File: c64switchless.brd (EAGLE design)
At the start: 22.8 x 45.4 mm, 12 parts, among them IC1 27C256, IC2 PIC12F629P

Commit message: updated with license
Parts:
- renumbered U$1 to SV4
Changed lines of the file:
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@@
 <attribute name="VALUE" x="-0.127" y="41.148" size="1.27" layer="27" ratio="10" rot="R270" display="off"/>
 </element>
-<element name="U$1" library="microchip" package="ICSP_MICROCHIP" value="ICSP_MICROCHIP" x="7.62" y="17.78" smashed="yes" rot="MR180">
+<element name="SV4" library="microchip" package="ICSP_MICROCHIP" value="ICSP_MICROCHIP" x="7.62" y="17.78" smashed="yes" rot="MR180">
 <attribute name="NAME" x="6.35" y="9.779" size="1.27" layer="26" ratio="10" rot="MR180" display="off"/>
 <attribute name="VALUE" x="6.35" y="27.051" size="1.27" layer="28" ratio="10" rot="MR180" display="off"/>
@@
 <vertex x="0" y="-1.27"/>
 </polygon>
-<contactref element="U$1" pad="3"/>
+<contactref element="SV4" pad="3"/>
 <polygon width="0.3048" layer="1" isolate="0.4064">
 <vertex x="0" y="44.45"/>
@@
 <wire x1="15.24" y1="35.56" x2="17.78" y2="35.56" width="0.8128" layer="16"/>
 <wire x1="5.08" y1="40.64" x2="17.78" y2="40.64" width="0.8128" layer="16"/>
-<contactref element="U$1" pad="2"/>
+<contactref element="SV4" pad="2"/>
 <wire x1="7.62" y1="13.97" x2="11.43" y2="17.78" width="0.254" layer="1"/>
 <wire x1="11.43" y1="17.78" x2="11.43" y2="31.75" width="0.254" layer="1"/>
@@
 <contactref element="IC2" pad="6"/>
 <contactref element="PAD2" pad="1"/>
-<contactref element="U$1" pad="5"/>
+<contactref element="SV4" pad="5"/>
 <wire x1="8.89" y1="29.21" x2="7.62" y2="30.48" width="0.1524" layer="1"/>
 <wire x1="8.89" y1="22.86" x2="8.89" y2="29.21" width="0.1524" layer="1"/>
@@
 <signal name="#RESTORE">
 <contactref element="PAD1" pad="1"/>
-<contactref element="U$1" pad="1"/>
+<contactref element="SV4" pad="1"/>
 <contactref element="IC2" pad="4"/>
 <wire x1="15.24" y1="27.94" x2="15.24" y2="22.86" width="0.254" layer="1"/>
@@
 </signal>
 <signal name="N$1">
-<contactref element="U$1" pad="4"/>
+<contactref element="SV4" pad="4"/>
 <contactref element="IC2" pad="7"/>
 <wire x1="6.35" y1="31.75" x2="7.62" y2="33.02" width="0.1524" layer="1"/>

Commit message: hole sizes
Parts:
- moved PAD2 0.32 mm to (5.40, 0.64)
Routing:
- net GND: track 2.54 -> 8.57 mm, vias 0 -> 2
- net N$1: track 15.0 -> 20.8 mm
- net N$22: track 10.2 -> 8.67 mm
- net N$24: track 30.6 -> 31.5 mm
- removed copper zone on layer 1, net GND
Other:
- board text added: "Rev 1.12"
- board text removed: "Rev 1.11"
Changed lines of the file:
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@@
 <text x="13.97" y="42.545" size="0.8128" layer="21" font="fixed" ratio="29">BWACK 2016</text>
 <text x="1.27" y="3.175" size="0.6096" layer="21" font="fixed">Quad Kernal Switch</text>
-<text x="1.27" y="-0.215" size="0.6096" layer="21">RESET</text>
+<text x="1.016" y="-0.215" size="0.6096" layer="21">RESET</text>
 <text x="9.525" y="-0.135" size="0.6096" layer="21">Restore</text>
 <text x="19.05" y="0" size="0.6096" layer="21" font="fixed" rot="R180">RGB LEDs</text>
-<text x="1.27" y="1.905" size="0.6096" layer="21" font="fixed">Rev 1.11</text>
+<text x="1.27" y="1.905" size="0.6096" layer="21" font="fixed">Rev 1.12</text>
 <text x="18.8595" y="5.3975" size="0.6096" layer="21" font="fixed">RED</text>
 <text x="13.2715" y="5.3975" size="0.6096" layer="21" font="fixed">GREEN</text>
@@
 <attribute name="VALUE" x="8.255" y="1.235" size="0.0254" layer="27"/>
 </element>
-<element name="PAD2" library="wirepad" package="1,6/0,9" value="" x="5.715" y="0.635" smashed="yes">
-<attribute name="NAME" x="4.953" y="1.651" size="0.6096" layer="25" ratio="10" display="off"/>
-<attribute name="VALUE" x="5.715" y="1.235" size="0.0254" layer="27"/>
+<element name="PAD2" library="wirepad" package="1,6/0,9" value="" x="5.3975" y="0.635" smashed="yes">
+<attribute name="NAME" x="4.6355" y="1.651" size="0.6096" layer="25" ratio="10" display="off"/>
+<attribute name="VALUE" x="5.3975" y="1.235" size="0.0254" layer="27"/>
 </element>
 <element name="R1" library="rcl" package="0207/10" value="2k" x="12.7" y="15.24" smashed="yes" rot="R90">
@@
 <contactref element="IC1" pad="20"/>
 <wire x1="2.54" y1="7.62" x2="5.08" y2="7.62" width="0.4064" layer="16"/>
-<polygon width="0.4064" layer="16" isolate="0.4064">
+<polygon width="0.4064" layer="16" isolate="0.3048">
 <vertex x="0" y="44.45"/>
 <vertex x="22.86" y="44.45"/>
@@
 </polygon>
 <contactref element="SV4" pad="3"/>
-<polygon width="0.3048" layer="1" isolate="0.4064">
-<vertex x="0" y="44.45"/>
-<vertex x="22.86" y="44.45"/>
-<vertex x="22.86" y="-1.27"/>
-<vertex x="0" y="-1.27"/>
-</polygon>
 <contactref element="SV3" pad="3"/>
 <contactref element="SV3" pad="4"/>
+<wire x1="10.16" y1="42.8625" x2="10.16" y2="39.37" width="1.27" layer="1"/>
+<wire x1="10.16" y1="39.37" x2="7.62" y2="39.37" width="1.27" layer="1"/>
+<via x="10.16" y="42.8625" extent="1-16" drill="0.6" shape="square"/>
+<via x="7.62" y="39.37" extent="1-16" drill="0.6" shape="square"/>
 </signal>
 <signal name="VCC">
@@
 <wire x1="5.08" y1="40.64" x2="17.78" y2="40.64" width="0.8128" layer="16"/>
 <contactref element="SV4" pad="2"/>
-<wire x1="7.62" y1="13.97" x2="11.43" y2="17.78" width="0.254" layer="1"/>
-<wire x1="11.43" y1="17.78" x2="11.43" y2="31.75" width="0.254" layer="1"/>
-<wire x1="11.43" y1="31.75" x2="15.24" y2="35.56" width="0.254" layer="1"/>
+<wire x1="7.62" y1="13.97" x2="11.43" y2="17.78" width="0.1524" layer="1"/>
+<wire x1="11.43" y1="17.78" x2="11.43" y2="31.75" width="0.1524" layer="1"/>
+<wire x1="11.43" y1="31.75" x2="15.24" y2="35.56" width="0.1524" layer="1"/>
 </signal>
 <signal name="N$2">
@@
 <wire x1="16.51" y1="39.37" x2="15.24" y2="38.1" width="0.1524" layer="1"/>
 <wire x1="21.59" y1="39.37" x2="16.51" y2="39.37" width="0.1524" layer="1"/>
-<wire x1="21.59" y1="32.385" x2="21.59" y2="39.37" width="0.1524" layer="1"/>
-<wire x1="19.05" y1="31.115" x2="21.59" y2="32.385" width="0.1524" layer="1"/>
-<wire x1="19.05" y1="29.21" x2="19.05" y2="31.115" width="0.1524" layer="1"/>
+<wire x1="21.59" y1="31.75" x2="21.59" y2="39.37" width="0.1524" layer="1"/>
+<wire x1="19.05" y1="31.75" x2="21.59" y2="31.75" width="0.1524" layer="1"/>
+<wire x1="19.05" y1="29.21" x2="19.05" y2="31.75" width="0.1524" layer="1"/>
 <wire x1="17.78" y1="27.94" x2="19.05" y2="29.21" width="0.1524" layer="1"/>
 </signal>
@@
 <contactref element="PAD2" pad="1"/>
 <contactref element="SV4" pad="5"/>
-<wire x1="8.89" y1="29.21" x2="7.62" y2="30.48" width="0.1524" layer="1"/>
-<wire x1="8.89" y1="22.86" x2="8.89" y2="29.21" width="0.1524" layer="1"/>
-<wire x1="7.62" y1="21.59" x2="8.89" y2="22.86" width="0.1524" layer="1"/>
-<wire x1="3.81" y1="2.54" x2="5.715" y2="0.635" width="0.254" layer="1"/>
-<wire x1="3.81" y1="2.54" x2="3.81" y2="16.51" width="0.254" layer="1"/>
-<wire x1="3.81" y1="16.51" x2="6.35" y2="16.51" width="0.254" layer="1"/>
-<wire x1="6.35" y1="16.51" x2="6.35" y2="17.78" width="0.254" layer="1"/>
-<wire x1="6.35" y1="17.78" x2="8.89" y2="17.78" width="0.254" layer="1"/>
-<wire x1="8.89" y1="17.78" x2="8.89" y2="20.32" width="0.254" layer="1"/>
-<wire x1="8.89" y1="20.32" x2="7.62" y2="21.59" width="0.254" layer="1"/>
+<wire x1="3.81" y1="2.54" x2="5.3975" y2="0.635" width="0.1524" layer="1"/>
+<wire x1="3.81" y1="2.54" x2="3.81" y2="16.51" width="0.1524" layer="1"/>
+<wire x1="3.81" y1="16.51" x2="6.35" y2="16.51" width="0.1524" layer="1"/>
+<wire x1="6.35" y1="16.51" x2="6.35" y2="17.78" width="0.1524" layer="1"/>
+<wire x1="6.35" y1="17.78" x2="8.89" y2="17.78" width="0.1524" layer="1"/>
+<wire x1="8.89" y1="17.78" x2="8.89" y2="20.32" width="0.1524" layer="1"/>
+<wire x1="8.89" y1="20.32" x2="7.62" y2="21.59" width="0.1524" layer="1"/>
+<wire x1="7.62" y1="30.48" x2="6.35" y2="29.21" width="0.1524" layer="1"/>
+<wire x1="6.35" y1="29.21" x2="6.35" y2="22.86" width="0.1524" layer="1"/>
+<wire x1="6.35" y1="22.86" x2="7.62" y2="21.59" width="0.1524" layer="1"/>
 </signal>
 <signal name="#RESTORE">
@@
 <contactref element="SV4" pad="1"/>
 <contactref element="IC2" pad="4"/>
-<wire x1="15.24" y1="27.94" x2="15.24" y2="22.86" width="0.254" layer="1"/>
-<wire x1="15.24" y1="22.86" x2="16.51" y2="21.59" width="0.254" layer="1"/>
-<wire x1="16.51" y1="21.59" x2="16.51" y2="19.05" width="0.254" layer="1"/>
-<wire x1="16.51" y1="19.05" x2="15.24" y2="17.78" width="0.254" layer="1"/>
-<wire x1="15.24" y1="17.78" x2="13.97" y2="17.78" width="0.254" layer="1"/>
-<wire x1="13.97" y1="17.78" x2="7.62" y2="11.43" width="0.254" layer="1"/>
-<wire x1="7.62" y1="11.43" x2="7.62" y2="6.35" width="0.254" layer="1"/>
-<wire x1="8.255" y1="0.635" x2="8.255" y2="5.715" width="0.254" layer="1"/>
-<wire x1="8.255" y1="5.715" x2="7.62" y2="6.35" width="0.254" layer="1"/>
+<wire x1="15.24" y1="27.94" x2="15.24" y2="22.86" width="0.1524" layer="1"/>
+<wire x1="15.24" y1="22.86" x2="16.51" y2="21.59" width="0.1524" layer="1"/>
+<wire x1="16.51" y1="21.59" x2="16.51" y2="19.05" width="0.1524" layer="1"/>
+<wire x1="16.51" y1="19.05" x2="15.24" y2="17.78" width="0.1524" layer="1"/>
+<wire x1="15.24" y1="17.78" x2="13.97" y2="17.78" width="0.1524" layer="1"/>
+<wire x1="13.97" y1="17.78" x2="7.62" y2="11.43" width="0.1524" layer="1"/>
+<wire x1="7.62" y1="11.43" x2="7.62" y2="6.35" width="0.1524" layer="1"/>
+<wire x1="8.255" y1="0.635" x2="8.255" y2="5.715" width="0.1524" layer="1"/>
+<wire x1="8.255" y1="5.715" x2="7.62" y2="6.35" width="0.1524" layer="1"/>
 </signal>
 <signal name="A13">
@@
 <contactref element="IC1" pad="26"/>
 <wire x1="19.05" y1="34.29" x2="20.32" y2="35.56" width="0.1524" layer="1"/>
-<wire x1="16.51" y1="34.29" x2="19.05" y2="34.29" width="0.1524" layer="1"/>
-<wire x1="16.51" y1="31.75" x2="16.51" y2="34.29" width="0.1524" layer="1"/>
+<wire x1="17.145" y1="34.29" x2="19.05" y2="34.29" width="0.1524" layer="1"/>
+<wire x1="16.51" y1="31.75" x2="16.51" y2="33.655" width="0.1524" layer="1"/>
+<wire x1="16.51" y1="33.655" x2="17.145" y2="34.29" width="0.1524" layer="1"/>
 <wire x1="15.24" y1="30.48" x2="16.51" y2="31.75" width="0.1524" layer="1"/>
 <wire x1="15.24" y1="20.32" x2="13.97" y2="21.59" width="0.4064" layer="1"/>
@@
 <contactref element="SV4" pad="4"/>
 <contactref element="IC2" pad="7"/>
-<wire x1="6.35" y1="31.75" x2="7.62" y2="33.02" width="0.1524" layer="1"/>
-<wire x1="6.35" y1="20.32" x2="6.35" y2="31.75" width="0.1524" layer="1"/>
-<wire x1="7.62" y1="19.05" x2="6.35" y2="20.32" width="0.1524" layer="1"/>
+<wire x1="7.62" y1="33.02" x2="6.35" y2="31.75" width="0.1524" layer="1"/>
+<wire x1="6.35" y1="31.75" x2="3.81" y2="31.75" width="0.1524" layer="1"/>
+<wire x1="3.81" y1="31.75" x2="3.81" y2="19.05" width="0.1524" layer="1"/>
+<wire x1="3.81" y1="19.05" x2="7.62" y2="19.05" width="0.1524" layer="1"/>
 </signal>
 <signal name="RED">
@@
 <contactref element="R3" pad="2"/>
 <contactref element="IC2" pad="5"/>
-<wire x1="7.62" y1="27.94" x2="10.16" y2="27.94" width="0.4064" layer="16"/>
-<wire x1="10.16" y1="27.94" x2="10.16" y2="20.32" width="0.4064" layer="16"/>
+<wire x1="10.16" y1="20.32" x2="10.16" y2="25.4" width="0.4064" layer="1"/>
+<wire x1="10.16" y1="25.4" x2="7.62" y2="27.94" width="0.4064" layer="1"/>
 </signal>
 <signal name="GREEN">
@@
 </signal>
 </signals>
+<errors>
+</errors>
 </board>
 </drawing>

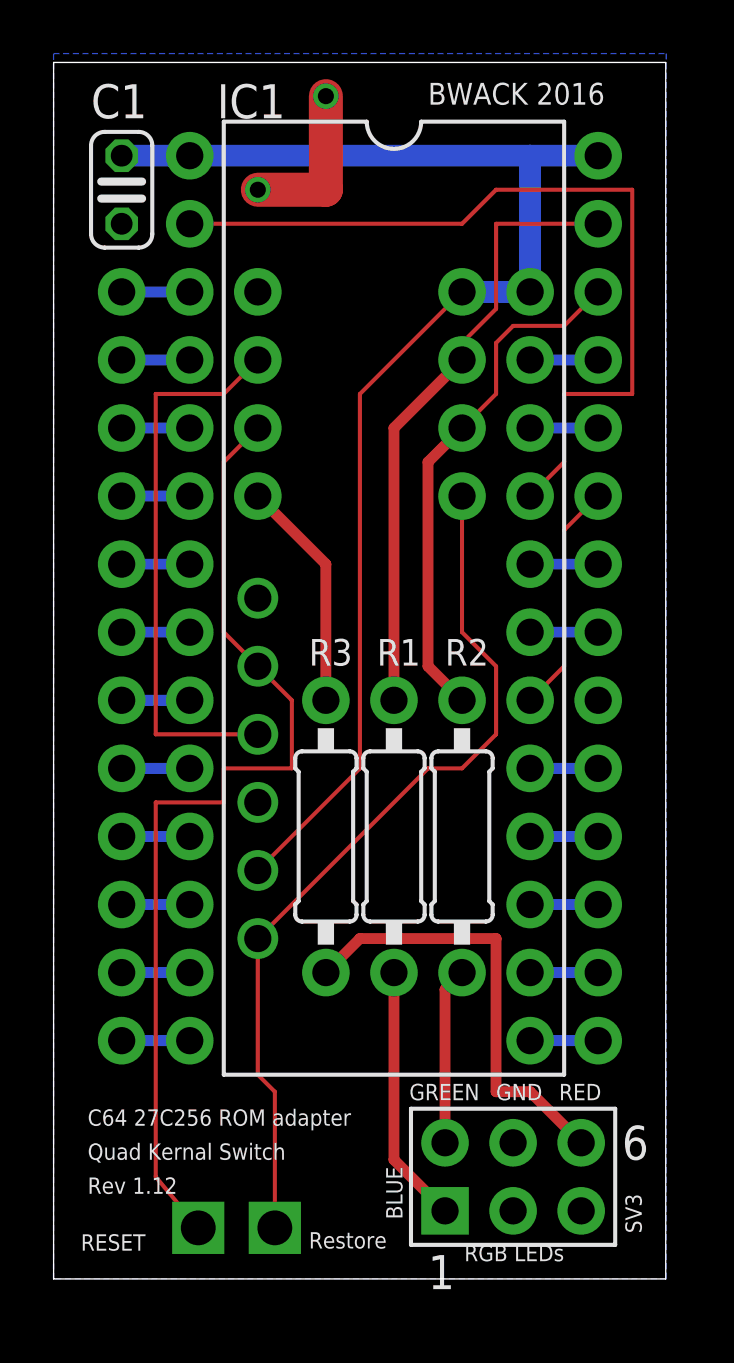
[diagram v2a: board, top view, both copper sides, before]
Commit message: Rev 1.13
Moved IC2 to clear space for the socket in the C64.
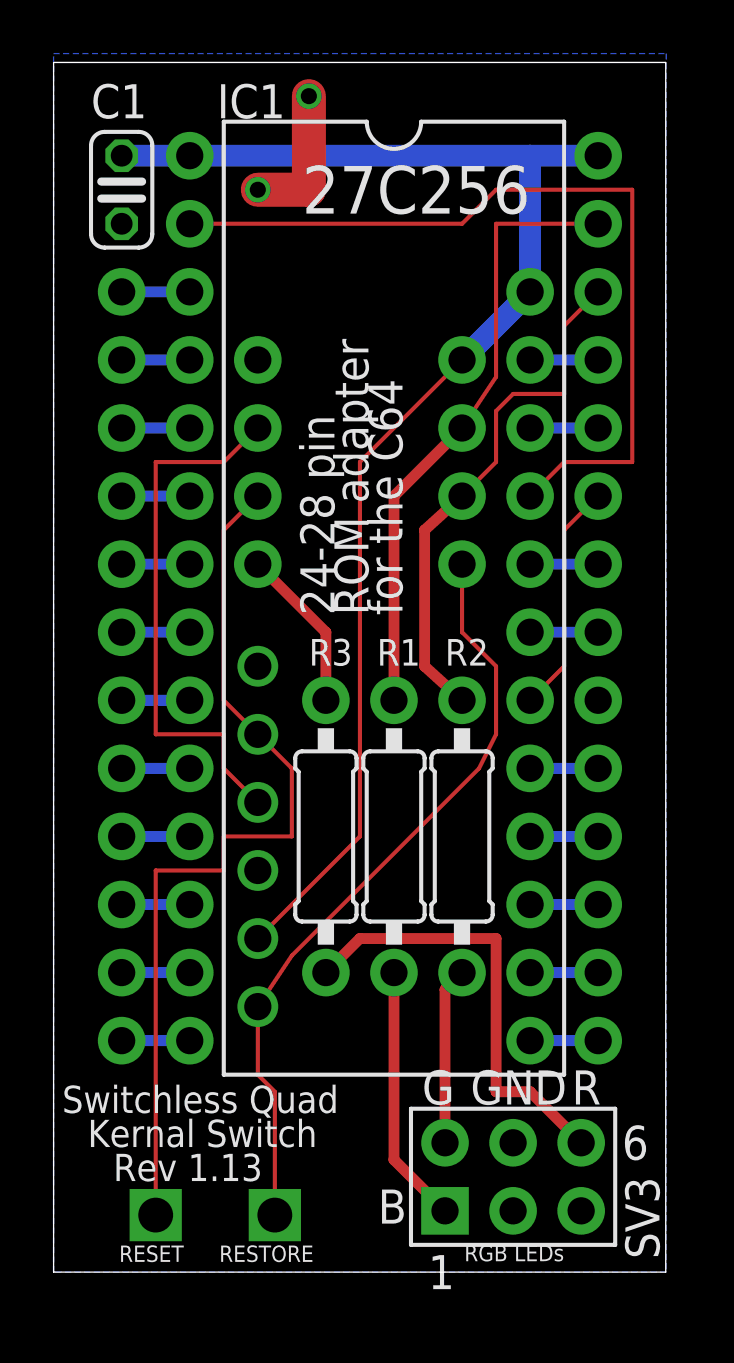
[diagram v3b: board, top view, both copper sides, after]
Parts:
- moved SV4 2.54 mm to (7.62, 15.2)
- moved IC2 2.54 mm to (11.4, 29.2)
- moved PAD2 1.66 mm to (3.81, 1.11)
- moved PAD1 0.48 mm to (8.26, 1.11)
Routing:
- net #RESTORE: track 32.5 -> 28.5 mm
- net #INTRST: track 37.1 -> 33.5 mm
- net N$22: track 8.67 -> 6.13 mm
- net VCC: track 50.1 -> 51.2 mm
- net N$1: track 20.8 -> 20.1 mm
- net GND: track 8.57 -> 7.94 mm
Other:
- board size 22.8 x 45.4 mm -> 22.8 x 45.1 mm
- board text added: "24-28 pin"
- board text added: "B"
- board text added: "G"
- board text added: "Kernal Switch"
- board text added: "R"
- board text added: "RESTORE"
- board text added: "ROM adapter"
- board text added: "Rev 1.13"
- board text added: "Switchless Quad"
- board text added: "for the C64"
- board text removed: "BLUE"
- board text removed: "C64 27C256 ROM adapter"
- board text removed: "GREEN"
- board text removed: "Quad Kernal Switch"
- board text removed: "RED"
- board text removed: "Restore"
- board text removed: "Rev 1.12"

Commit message: resistor values
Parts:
- R1: value 2k -> 1k
- R2: value 2k -> 3k3
- R3: value 2k -> 560R
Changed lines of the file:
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@@
 <attribute name="VALUE" x="3.81" y="1.71125" size="0.0254" layer="27"/>
 </element>
-<element name="R1" library="rcl" package="0207/10" value="2k" x="12.7" y="15.24" smashed="yes" rot="R90">
+<element name="R1" library="rcl" package="0207/10" value="1k" x="12.7" y="15.24" smashed="yes" rot="R90">
 <attribute name="NAME" x="12.065" y="21.6154" size="0.9906" layer="25" ratio="10"/>
 <attribute name="VALUE" x="13.1826" y="13.6144" size="0.9906" layer="27" ratio="10" rot="R90"/>
 </element>
-<element name="R2" library="rcl" package="0207/10" value="2k" x="15.24" y="15.24" smashed="yes" rot="R90">
+<element name="R2" library="rcl" package="0207/10" value="3k3" x="15.24" y="15.24" smashed="yes" rot="R90">
 <attribute name="NAME" x="14.605" y="21.6154" size="0.9906" layer="25" ratio="10"/>
 <attribute name="VALUE" x="15.7226" y="13.6144" size="0.9906" layer="27" ratio="10" rot="R90"/>
 </element>
-<element name="R3" library="rcl" package="0207/10" value="2k" x="10.16" y="15.24" smashed="yes" rot="R90">
+<element name="R3" library="rcl" package="0207/10" value="560R" x="10.16" y="15.24" smashed="yes" rot="R90">
 <attribute name="NAME" x="9.525" y="21.6154" size="0.9906" layer="25" ratio="10"/>
 <attribute name="VALUE" x="10.6426" y="13.6144" size="0.9906" layer="27" ratio="10" rot="R90"/>
